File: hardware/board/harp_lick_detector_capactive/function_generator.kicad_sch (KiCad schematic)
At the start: 10 parts, among them U6 LTC6263, U9 AD9833xRM

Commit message: remove hand-soldering footprints
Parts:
- R20, R22, R26: footprint Resistor_SMD:R_0402_1005Metric_Pad0.72x0.64mm_HandSolder -> Resistor_SMD:R_0402_1005Metric
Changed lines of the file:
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@@
       (effects (font (size 1.27 1.27)))
     )
-    (property "Footprint" "Resistor_SMD:R_0402_1005Metric_Pad0.72x0.64mm_HandSolder" (at 186.563 114.3 90)
+    (property "Footprint" "Resistor_SMD:R_0402_1005Metric" (at 186.563 114.3 90)
       (effects (font (size 1.27 1.27)) hide)
     )
@@
       (effects (font (size 1.27 1.27)) (justify left))
     )
-    (property "Footprint" "Resistor_SMD:R_0402_1005Metric_Pad0.72x0.64mm_HandSolder" (at 163.322 114.3 90)
+    (property "Footprint" "Resistor_SMD:R_0402_1005Metric" (at 163.322 114.3 90)
       (effects (font (size 1.27 1.27)) hide)
     )
@@
       (effects (font (size 1.27 1.27)))
     )
-    (property "Footprint" "Resistor_SMD:R_0402_1005Metric_Pad0.72x0.64mm_HandSolder" (at 166.878 102.87 90)
-      (effects (font (size 1.27 1.27)) hide)
-    )
+    (property "Footprint" "Resistor_SMD:R_0402_1005Metric" (at 166.878 102.87 90)
+      (effects (font (size 1.27 1.27)) hide)
+    )

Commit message: update footprints; populate bom
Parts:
- C33: Notes 200mOhm ESR @ 100KHz, marking on positive side -> 200mOhm ESR @ 100KHz, band marking on positive side
- C34, C35, C36: footprint Capacitor_SMD:C_0402_1005Metric_Pad0.74x0.62mm_HandSolder -> Capacitor_SMD:C_0402_1005Metric
- R26: value 320 -> 330; Link https://www.digikey.com/en/products/detail/koa-speer-electr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 -> https://www.digikey.com/en/products/detail/panasonic-electr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; Manufacturer KOA Speer Electronics, Inc. -> Panasonic Electronic Components; Manufacturer Number RN73R1ETTP3200B25 -> ERA-2AEB331X; Vendor Number 2019-RN73R1ETTP3200B25DKR-ND -> (none)
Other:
- note added: "12MHz crystal X1 is shared between RP2040 (U4) and AD9833 (U9)."
- note added: "Vout_min = 330/(330 + 10e3) * 650 = 21[mVpp] signal"
- note removed: "Vout_min = 320/(320 + 10e3) * 650 = 20[mVpp] signal"
- company: (none) -> The Allen Institute for Neural Dynamics
- title: (none) -> Lickety Split Capacitive Lick Detector
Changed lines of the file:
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@@
 (kicad_sch (version 20230121) (generator eeschema)
   (paper "A4")
+  (title_block
+    (title "Lickety Split Capacitive Lick Detector")
+    (date "2023-09-01")
+    (rev "0.5")
+    (company "The Allen Institute for Neural Dynamics")
+  )
   (junction (at 165.1 108.585) (diameter 0) (color 0 0 0 0)
   )
@@
     (effects (font (size 1.27 1.27)) (justify left bottom))
   )
-  (text "Vout_min = 320/(320 + 10e3) * 650 = 20[mVpp] signal"
+  (text "Vout_min = 330/(330 + 10e3) * 650 = 21[mVpp] signal"
     (at 172.72 76.2 0)
     (effects (font (size 1.27 1.27)) (justify left bottom))
@@
   )
   (text "Buffer" (at 201.295 102.87 0)
+    (effects (font (size 1.27 1.27)) (justify left bottom))
+  )
+  (text "12MHz crystal X1 is shared between \nRP2040 (U4) and AD9833 (U9)."
+    (at 58.42 100.965 0)
     (effects (font (size 1.27 1.27)) (justify left bottom))
   )
@@
       (effects (font (size 1.27 1.27)) (justify right))
     )
-    (property "Footprint" "Capacitor_SMD:C_0402_1005Metric_Pad0.74x0.62mm_HandSolder" (at 151.4348 81.28 0)
+    (property "Footprint" "Capacitor_SMD:C_0402_1005Metric" (at 151.4348 81.28 0)
       (effects (font (size 1.27 1.27)) hide)
     )
@@
       (effects (font (size 1.27 1.27)) hide)
     )
-    (property "Notes" "200mOhm ESR @ 100KHz, marking on positive side" (at 38.1 175.26 0)
+    (property "Notes" "200mOhm ESR @ 100KHz, band marking on positive side" (at 38.1 175.26 0)
       (effects (font (size 1.27 1.27)) hide)
     )
@@
       (effects (font (size 1.27 1.27)) (justify left))
     )
-    (property "Value" "320" (at 165.1 115.57 90)
+    (property "Value" "330" (at 165.1 115.57 90)
       (effects (font (size 1.27 1.27)) (justify left))
     )
@@
       (effects (font (size 1.27 1.27)) hide)
     )
-    (property "Datasheet" "https://mm.digikey.com/Volume0/opasdata/d220001/medias/docus/323/RN73R_Type_DS.pdf" (at 165.1 114.3 0)
-      (effects (font (size 1.27 1.27)) hide)
-    )
-    (property "Link" "https://www.digikey.com/en/products/detail/koa-speer-electronics-inc/RN73R1ETTP3200B25/10003722" (at 165.1 114.3 0)
-      (effects (font (size 1.27 1.27)) hide)
-    )
-    (property "Manufacturer" "KOA Speer Electronics, Inc." (at 165.1 114.3 0)
-      (effects (font (size 1.27 1.27)) hide)
-    )
-    (property "Manufacturer Number" "RN73R1ETTP3200B25" (at 165.1 114.3 0)
+    (property "Datasheet" "https://industrial.panasonic.com/cdbs/www-data/pdf/RDM0000/AOA0000C307.pdf" (at 165.1 114.3 0)
+      (effects (font (size 1.27 1.27)) hide)
+    )
+    (property "Link" "https://www.digikey.com/en/products/detail/panasonic-electronic-components/ERA-2AEB331X/1705993" (at 165.1 114.3 0)
+      (effects (font (size 1.27 1.27)) hide)
+    )
+    (property "Manufacturer" "Panasonic Electronic Components" (at 165.1 114.3 0)
+      (effects (font (size 1.27 1.27)) hide)
+    )
+    (property "Manufacturer Number" "ERA-2AEB331X" (at 165.1 114.3 0)
       (effects (font (size 1.27 1.27)) hide)
     )
@@
       (effects (font (size 1.27 1.27)) hide)
     )
-    (property "Vendor Number" "2019-RN73R1ETTP3200B25DKR-ND" (at 165.1 114.3 0)
+    (property "Vendor Number" "" (at 165.1 114.3 0)
       (effects (font (size 1.27 1.27)) hide)
     )
@@
       (effects (font (size 1.27 1.27)) (justify left))
     )
-    (property "Footprint" "Capacitor_SMD:C_0402_1005Metric_Pad0.74x0.62mm_HandSolder" (at 128.27 75.2348 0)
+    (property "Footprint" "Capacitor_SMD:C_0402_1005Metric" (at 128.27 75.2348 0)
       (effects (font (size 1.27 1.27)) hide)
     )
@@
       (effects (font (size 1.27 1.27)) (justify left))
     )
-    (property "Footprint" "Capacitor_SMD:C_0402_1005Metric_Pad0.74x0.62mm_HandSolder" (at 44.7548 171.45 0)
-      (effects (font (size 1.27 1.27)) hide)
-    )
+    (property "Footprint" "Capacitor_SMD:C_0402_1005Metric" (at 44.7548 171.45 0)
+      (effects (font (size 1.27 1.27)) hide)
+    )

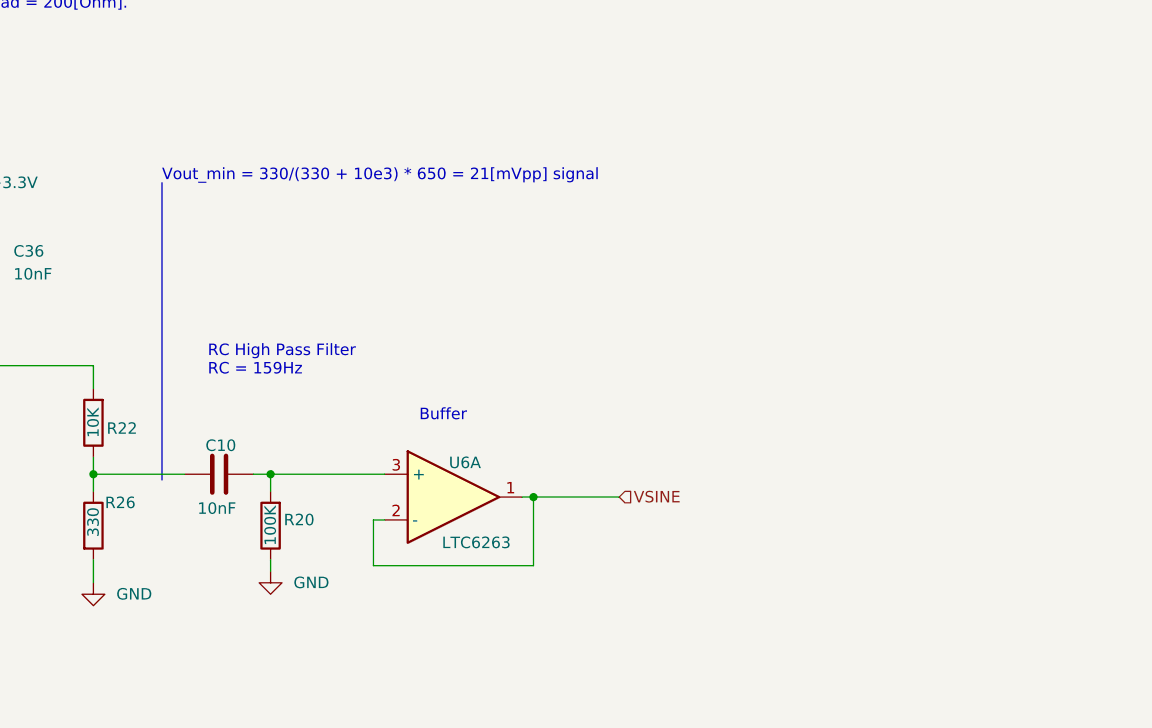
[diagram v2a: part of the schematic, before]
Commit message: add tvs diodes; remove run pullup; finish trace guard
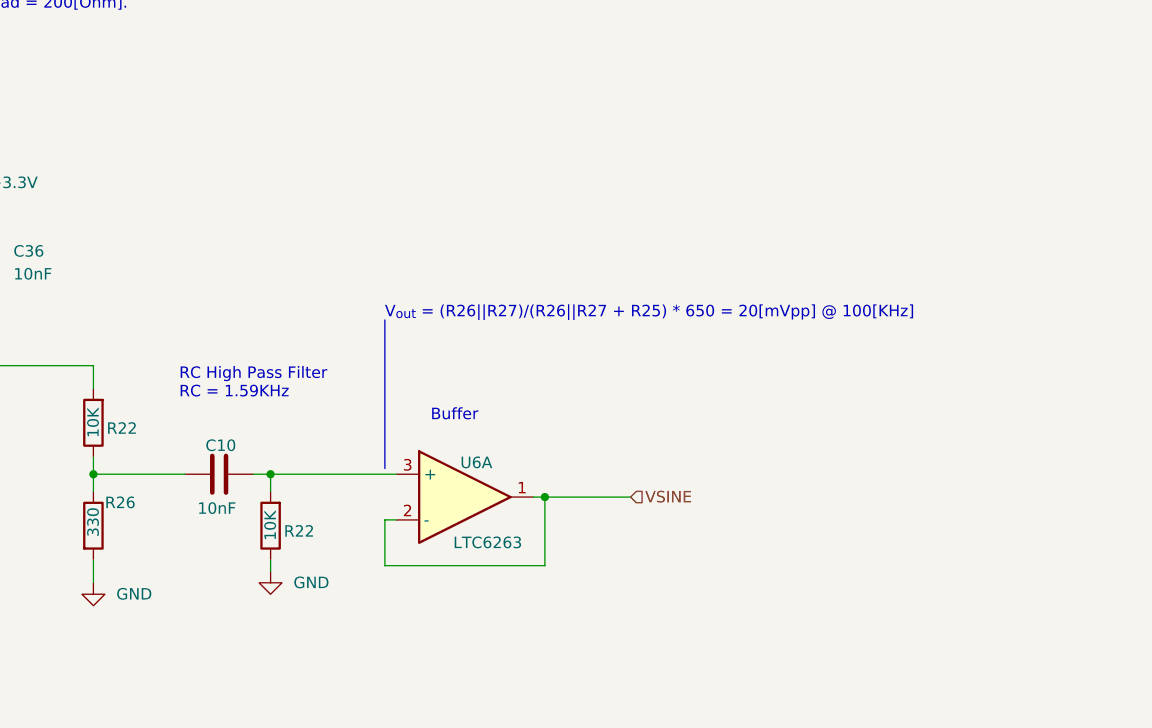
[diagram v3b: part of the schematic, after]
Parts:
- removed R20: 100K, Resistor_SMD:R_0402_1005Metric, symbol Device:R
- added R22: 10K, Resistor_SMD:R_0402_1005Metric, symbol Device:R
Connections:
- net GND: now also R22.1
- net at C10.2, U6.3 (+): now also R22.2
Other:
- note added: "RC High Pass Filter RC = 1.59KHz"
- note added: "V_{out} = (R26||R27)/(R26||R27 + R25) * 650 = 20[mVpp] @ 100[KHz]"
- note removed: "RC High Pass Filter RC = 159Hz"
- note removed: "Vout_min = 330/(330 + 10e3) * 650 = 21[mVpp] signal"
- moved on the sheet: U6A
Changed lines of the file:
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@@
   (junction (at 165.1 108.585) (diameter 0) (color 0 0 0 0)
   )
-  (junction (at 213.995 111.125) (diameter 0) (color 0 0 0 0)
+  (junction (at 215.265 111.125) (diameter 0) (color 0 0 0 0)
   )
   (junction (at 134.62 107.95) (diameter 0) (color 0 0 0 0)
@@
     (stroke (width 0) (type default))
   )
-  (wire (pts (xy 213.995 111.125) (xy 213.995 118.745))
+  (wire (pts (xy 215.265 111.125) (xy 215.265 118.745))
     (stroke (width 0) (type default))
   )
@@
     (stroke (width 0) (type default))
   )
-  (wire (pts (xy 184.785 108.585) (xy 197.485 108.585))
-    (stroke (width 0) (type default))
-  )
-  (wire (pts (xy 196.215 113.665) (xy 196.215 118.745))
+  (polyline (pts (xy 197.485 91.44) (xy 197.485 107.95))
+    (stroke (width 0) (type default))
+  )
+  (wire (pts (xy 184.785 108.585) (xy 198.755 108.585))
+    (stroke (width 0) (type default))
+  )
+  (wire (pts (xy 197.485 113.665) (xy 197.485 118.745))
     (stroke (width 0) (type default))
   )
@@
     (stroke (width 0) (type default))
   )
-  (wire (pts (xy 196.215 118.745) (xy 213.995 118.745))
+  (wire (pts (xy 197.485 118.745) (xy 215.265 118.745))
     (stroke (width 0) (type default))
   )
@@
     (stroke (width 0) (type default))
   )
-  (wire (pts (xy 213.995 111.125) (xy 223.52 111.125))
-    (stroke (width 0) (type default))
-  )
-  (wire (pts (xy 197.485 113.665) (xy 196.215 113.665))
-    (stroke (width 0) (type default))
-  )
-  (wire (pts (xy 213.995 111.125) (xy 212.725 111.125))
+  (wire (pts (xy 215.265 111.125) (xy 224.79 111.125))
+    (stroke (width 0) (type default))
+  )
+  (wire (pts (xy 198.755 113.665) (xy 197.485 113.665))
+    (stroke (width 0) (type default))
+  )
+  (wire (pts (xy 215.265 111.125) (xy 213.995 111.125))
     (stroke (width 0) (type default))
   )
@@
     (stroke (width 0) (type default))
   )
-  (polyline (pts (xy 172.72 76.2) (xy 172.72 109.22))
-    (stroke (width 0) (type default))
-  )
-  (text "RC High Pass Filter\nRC = 159Hz" (at 177.8 97.79 0)
+  (text "RC High Pass Filter\nRC = 1.59KHz" (at 174.625 100.33 0)
     (effects (font (size 1.27 1.27)) (justify left bottom))
   )
@@
     (effects (font (size 1.27 1.27)) (justify left bottom))
   )
-  (text "Vout_min = 330/(330 + 10e3) * 650 = 21[mVpp] signal"
-    (at 172.72 76.2 0)
+  (text "V_{out} = (R26||R27)/(R26||R27 + R25) * 650 = 20[mVpp] @ 100[KHz]"
+    (at 197.485 91.44 0)
     (effects (font (size 1.27 1.27)) (justify left bottom))
   )
@@
     (effects (font (size 1.27 1.27)) (justify left bottom))
   )
-  (text "Buffer" (at 201.295 102.87 0)
+  (text "Buffer" (at 202.565 102.87 0)
     (effects (font (size 1.27 1.27)) (justify left bottom))
   )
@@
     (effects (font (size 1.27 1.27)) (justify right))
   )
-  (hierarchical_label "VSINE" (shape input) (at 223.52 111.125 0) (fields_autoplaced)
+  (hierarchical_label "VSINE" (shape input) (at 224.79 111.125 0) (fields_autoplaced)
     (effects (font (size 1.27 1.27)) (justify left))
   )
   (hierarchical_label "SCK" (shape input) (at 118.11 88.9 180) (fields_autoplaced)
     (effects (font (size 1.27 1.27)) (justify right))
-  )
-  (symbol (lib_id "Device:R") (at 184.785 114.3 180) (unit 1)
-    (in_bom yes) (on_board yes) (dnp no)
-    (property "Reference" "R20" (at 187.96 113.665 0)
-      (effects (font (size 1.27 1.27)))
-    )
-    (property "Value" "100K" (at 184.785 114.3 90)
-      (effects (font (size 1.27 1.27)))
-    )
-    (property "Footprint" "Resistor_SMD:R_0402_1005Metric" (at 186.563 114.3 90)
-      (effects (font (size 1.27 1.27)) hide)
-    )
-    (property "Datasheet" "https://www.yageo.com/upload/media/product/productsearch/datasheet/rchip/PYu-RT_1-to-0.01_RoHS_L_15.pdf" (at 184.785 114.3 0)
-      (effects (font (size 1.27 1.27)) hide)
-    )
-    (property "Link" "https://www.digikey.com/en/products/detail/yageo/RT0402BRD07100KL/1068989" (at 184.785 114.3 0)
-      (effects (font (size 1.27 1.27)) hide)
-    )
-    (property "Manufacturer" "Yageo" (at 184.785 114.3 0)
-      (effects (font (size 1.27 1.27)) hide)
-    )
-    (property "Manufacturer Number" "RT0402BRD07100KL" (at 184.785 114.3 0)
-      (effects (font (size 1.27 1.27)) hide)
-    )
-    (property "Notes" "" (at 184.785 114.3 0)
-      (effects (font (size 1.27 1.27)) hide)
-    )
-    (property "Tolerance" "0.1%" (at 184.785 114.3 0)
-      (effects (font (size 1.27 1.27)) hide)
-    )
-    (pin "1")
-    (pin "2")
-    (instances
-      (project "harp_lick_detector_capactive"
-        (path "/e63e39d7-6ac0-4ffd-8aa3-1841a4541b55/8b2c79bc-d662-4528-ac6e-e4616ba8e8ad"
-          (reference "R20") (unit 1)
-        )
-        (path "/e63e39d7-6ac0-4ffd-8aa3-1841a4541b55/4df88917-387d-4e6a-a0c2-9efea845a08d"
-          (reference "R27") (unit 1)
-        )
-      )
-    )
   )
   (symbol (lib_id "power:GND") (at 165.1 120.65 0) (unit 1)
@@
     )
   )
-  (symbol (lib_id "kicad_component_library:LTC6263") (at 202.565 111.125 0) (unit 1)
-    (in_bom yes) (on_board yes) (dnp no)
-    (property "Reference" "U6" (at 206.375 107.315 0)
-      (effects (font (size 1.27 1.27)))
-    )
-    (property "Value" "LTC6263" (at 207.645 116.205 0)
-      (effects (font (size 1.27 1.27)))
-    )
-    (property "Footprint" "Package_SO:MSOP-16_3x4mm_P0.5mm" (at 224.79 117.475 0)
-      (effects (font (size 1.27 1.27)) hide)
-    )
-    (property "Datasheet" "https://www.analog.com/media/en/technical-documentation/data-sheets/626123fa.pdf" (at 250.19 119.38 0)
-      (effects (font (size 1.27 1.27)) hide)
-    )
-    (property "Link" "https://www.digikey.com/en/products/detail/analog-devices-inc/LTC6263IMS-PBF/6596388" (at 202.565 111.125 0)
-      (effects (font (size 1.27 1.27)) hide)
-    )
-    (property "Manufacturer" "Analog Devices Inc." (at 202.565 111.125 0)
-      (effects (font (size 1.27 1.27)) hide)
-    )
-    (property "Manufacturer Number" "LTC6263IMS#PBF" (at 202.565 111.125 0)
+  (symbol (lib_id "kicad_component_library:LTC6263") (at 203.835 111.125 0) (unit 1)
+    (in_bom yes) (on_board yes) (dnp no)
+    (property "Reference" "U6" (at 207.645 107.315 0)
+      (effects (font (size 1.27 1.27)))
+    )
+    (property "Value" "LTC6263" (at 208.915 116.205 0)
+      (effects (font (size 1.27 1.27)))
+    )
+    (property "Footprint" "Package_SO:MSOP-16_3x4mm_P0.5mm" (at 226.06 117.475 0)
+      (effects (font (size 1.27 1.27)) hide)
+    )
+    (property "Datasheet" "https://www.analog.com/media/en/technical-documentation/data-sheets/626123fa.pdf" (at 251.46 119.38 0)
+      (effects (font (size 1.27 1.27)) hide)
+    )
+    (property "Link" "https://www.digikey.com/en/products/detail/analog-devices-inc/LTC6263IMS-PBF/6596388" (at 203.835 111.125 0)
+      (effects (font (size 1.27 1.27)) hide)
+    )
+    (property "Manufacturer" "Analog Devices Inc." (at 203.835 111.125 0)
+      (effects (font (size 1.27 1.27)) hide)
+    )
+    (property "Manufacturer Number" "LTC6263IMS#PBF" (at 203.835 111.125 0)
       (effects (font (size 1.27 1.27)) hide)
     )
@@
         )
       )
+    )
+  )
+  (symbol (lib_id "Device:R") (at 184.785 114.3 180) (unit 1)
+    (in_bom yes) (on_board yes) (dnp no)
+    (property "Reference" "R22" (at 187.96 114.935 0)
+      (effects (font (size 1.27 1.27)))
+    )
+    (property "Value" "10K" (at 184.785 114.3 90)
+      (effects (font (size 1.27 1.27)))
+    )
+    (property "Footprint" "Resistor_SMD:R_0402_1005Metric" (at 186.563 114.3 90)
+      (effects (font (size 1.27 1.27)) hide)
+    )
+    (property "Datasheet" "https://www.yageo.com/upload/media/product/productsearch/datasheet/rchip/PYu-RT_1-to-0.01_RoHS_L_15.pdf" (at 184.785 114.3 0)
+      (effects (font (size 1.27 1.27)) hide)
+    )
+    (property "Link" "https://www.digikey.com/en/products/detail/yageo/RT0402BRD0710KL/1068998" (at 184.785 114.3 0)
+      (effects (font (size 1.27 1.27)) hide)
+    )
+    (property "Manufacturer" "Yageo" (at 184.785 114.3 0)
+      (effects (font (size 1.27 1.27)) hide)
+    )
+    (property "Manufacturer Number" "RT0402BRD0710KL" (at 184.785 114.3 0)
+      (effects (font (size 1.27 1.27)) hide)
+    )
+    (property "Tolerance" "0.1%" (at 184.785 114.3 0)
+      (effects (font (size 1.27 1.27)) hide)
+    )
+    (property "Temperature Coefficient" "25ppm/C" (at 184.785 114.3 90)
+      (effects (font (size 1.27 1.27)) hide)
+    )
+    (pin "1")
+    (pin "2")
+    (instances
+      (project "harp_lick_detector_capactive"
+        (path "/e63e39d7-6ac0-4ffd-8aa3-1841a4541b55/8b2c79bc-d662-4528-ac6e-e4616ba8e8ad"
+          (reference "R22") (unit 1)
+        )
+        (path "/e63e39d7-6ac0-4ffd-8aa3-1841a4541b55/4df88917-387d-4e6a-a0c2-9efea845a08d"
+          (reference "R27") (unit 1)
+        )
+      )

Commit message: draft v0.6.0 board
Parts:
- removed C10, C36: 10nF, Capacitor_SMD:C_0402_1005Metric, symbol Device:C
- removed C33: 10uF, Capacitor_SMD:C_0805_2012Metric_Pad1.18x1.45mm_HandSolder, symbol Device:C_Polarized
- removed C34, C35: 100nF, Capacitor_SMD:C_0402_1005Metric, symbol Device:C
- removed R22 (x2): 10K, Resistor_SMD:R_0402_1005Metric, symbol Device:R
- removed R26: 330, Resistor_SMD:R_0402_1005Metric, symbol Device:R
- removed U9: AD9833xRM, Package_SO:MSOP-10_3x3mm_P0.5mm, symbol Interface:AD9833xRM
- added C10 (x5): 1nF, Capacitor_SMD:C_0402_1005Metric, symbol Device:C
- added R16, R17, R25, R45, R8: 4K7, Resistor_SMD:R_0402_1005Metric, symbol Device:R
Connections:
- net GND: now also C10.2, C10.2, C10.2, C10.2, R25.2
- net at U6.3 (+): now also C10.2, R25.1
- new net: C10.1, R16.1, R8.2
- new net: C10.1, R16.2, R17.1
- new net: C10.1, R17.2, R45.1
- new net: C10.1, C10.1, R45.2
- new net 100KHZ_SQ_WAVE_IN: R8.1
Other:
- note added: "RC High Pass Filter DC Offset Removal"
- note added: "Reduce 3.3V, 100KHz square wave from the RP2040 to approximate a 20mV, 100KHz sine wave."
- note added: "V_{out} = 20[mVpp] @ 100[KHz]"
- note removed: "10uF tantalum"
- note removed: "12MHz crystal X1 is shared between RP2040 (U4) and AD9833 (U9)."
- note removed: "AD9833 outputs a 650[mV] signal with a 325[mV] offset. Vout has an internal load resistor RLoad = 200[Ohm]."
- note removed: "Datasheet: "Digital and analog ground planes should be joined in one place only." If the AD9833 is the only device requiring split grounds, join the AD9833 AGND and DGND pins."
- note removed: "Function Generator Bypass Caps"
- note removed: "RC High Pass Filter RC = 1.59KHz"
- note removed: "V_{out} = (R26||R27)/(R26||R27 + R25) * 650 = 20[mVpp] @ 100[KHz]"
- moved on the sheet: U6A

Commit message: draft v0.7 pcb schematic and layout
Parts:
- removed U6: LTC6263, Package_SO:MSOP-16_3x4mm_P0.5mm, symbol kicad_component_library:LTC6263
- added C20 (x2), C21: 100nF, Capacitor_SMD:C_0402_1005Metric, symbol Device:C
- added R21: 100K, Resistor_SMD:R_0402_1005Metric, symbol Device:R
- added R49 (x2): 1K00, Resistor_SMD:R_0402_1005Metric, symbol Device:R
- added R50: 2K2, Resistor_SMD:R_0402_1005Metric, symbol Device:R
- added U16: AD8615, Package_TO_SOT_SMD:TSOT-23-5, symbol kicad_component_library:AD8615
- added U18: TS5A9411DCKR, Package_TO_SOT_SMD:SOT-363_SC-70-6, symbol kicad_component_library:TS5A9411DCKR
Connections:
- net GND: now also C20.1, C20.1, C21.2, R49.2, U18.3 (GND)
- net VSINE: now also R21.2, R49.2, U16.1
- net at C10.1, R16.1, R8.2: now also R50.2
- net at C10.2, R25.1: now also U16.3 (+)
- net 100KHZ_SQ_WAVE_IN renamed 100KHZ_IN
- new net: R49.1, U18.4
- new net: U16.4 (-), U18.5
- new net: R21.1, R49.1, U18.6
- new net +2V5: C20.2, U16.5 (V+)
- new net +3V3: C20.2, U18.2 (Vcc)
- new net -2V5: C21.1, U16.2 (V-)
- new net 125KHZ_IN: R50.1
- new net GAIN_SEL: U18.1
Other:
- note added: "100KHz or 125KHz Square-to-Sine wave Front-End with 20mVpp amplitude."
- note added: "1x-or-101x Gain"
- note added: "3.3V, 100KHz or 125KHz input square wave from RP2040. Only one option is enabled at a time while the other option is set to input. (note: rp2040 gpio pins do not support tri-state option.)"
- note added: "U17 Bypass Caps"
- note added: "U18 Bypass Cap"
- note removed: "Buffer"
- note removed: "Reduce 3.3V, 100KHz square wave from the RP2040 to approximate a 20mV, 100KHz sine wave."
- moved on the sheet: C10, R25, R8
